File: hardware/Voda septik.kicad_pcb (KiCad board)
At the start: 2 copper layers, 1 part, among them U1 ESP32-DevKitC-30

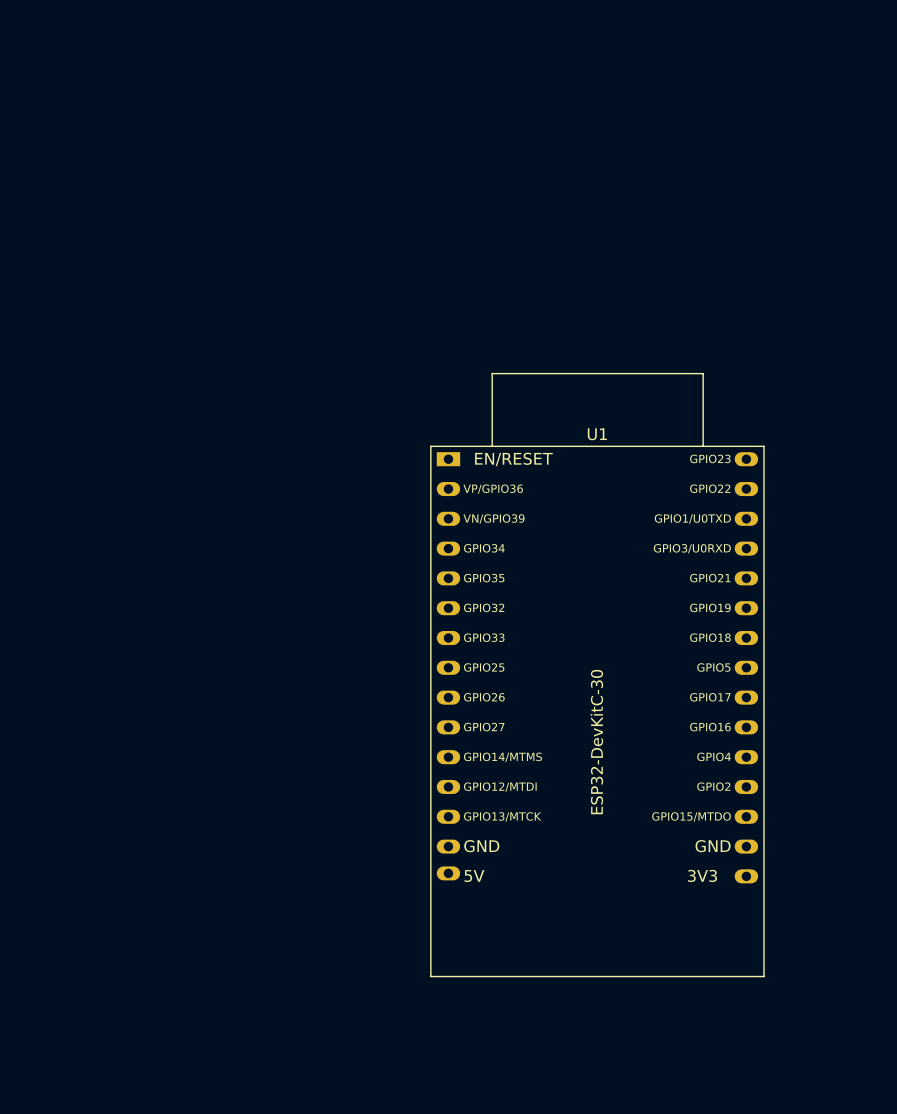
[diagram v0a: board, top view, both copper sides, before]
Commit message: Dokončení schématu a návrhu PCB o stavu, který byl poslán do výroby.
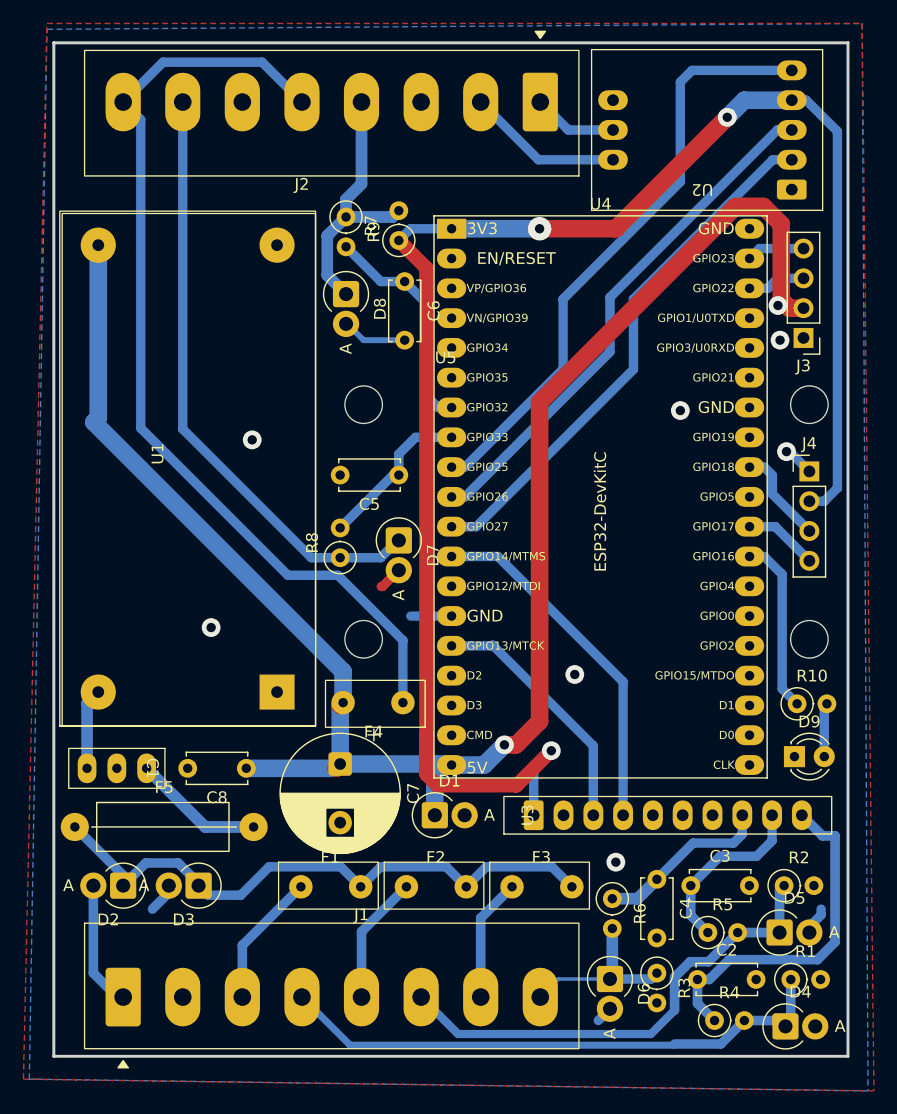
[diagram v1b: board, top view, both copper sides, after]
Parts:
- added C1: 100n, martin:Odruseni_3x_2.54mm, F.Cu at (98.8, 117.3)
- added C2: 100n, Capacitor_THT:C_Disc_D5.0mm_W2.5mm_P5.00mm, F.Cu at (145.7, 135.3)
- added C3: 100n, Capacitor_THT:C_Disc_D5.0mm_W2.5mm_P5.00mm, F.Cu at (145.2, 127.3)
- added C4: 100n, Capacitor_THT:C_Disc_D5.0mm_W2.5mm_P5.00mm, F.Cu at (142.3, 126.8)
- added C5: 1n, Capacitor_THT:C_Disc_D5.0mm_W2.5mm_P5.00mm, F.Cu at (120.3, 92.3)
- added C6: 100p, Capacitor_THT:C_Disc_D5.0mm_W2.5mm_P5.00mm, F.Cu at (120.8, 75.8)
- added C7: 470u, Capacitor_THT:CP_Radial_D10.0mm_P5.00mm, F.Cu at (115.3, 117.0)
- added C8: 100n, Capacitor_THT:C_Disc_D5.0mm_W2.5mm_P5.00mm, F.Cu at (107.3, 117.3)
- added D1: BZW04-5V8, Diode_THT:D_DO-15_P2.54mm_Vertical_AnodeUp, F.Cu at (123.3, 121.3)
- added D2: 1N4007, Diode_THT:D_DO-15_P2.54mm_Vertical_AnodeUp, F.Cu at (96.8, 127.3)
- added D3: BZW06-26, Diode_THT:D_DO-15_P2.54mm_Vertical_AnodeUp, F.Cu at (103.2, 127.3)
- added D4: BZW04-5V8, Diode_THT:D_DO-15_P2.54mm_Vertical_AnodeUp, F.Cu at (153.2, 139.3)
- added D5: BZW04-5V8, Diode_THT:D_DO-15_P2.54mm_Vertical_AnodeUp, F.Cu at (152.7, 131.3)
- added D6: BZW04-5V8, Diode_THT:D_DO-15_P2.54mm_Vertical_AnodeUp, F.Cu at (138.3, 135.3)
- added D7: BZW04-5V8, Diode_THT:D_DO-15_P2.54mm_Vertical_AnodeUp, F.Cu at (120.3, 97.9)
- added D8: BZW04-5V8, Diode_THT:D_DO-15_P2.54mm_Vertical_AnodeUp, F.Cu at (115.8, 76.9)
- added D9: LED, LED_THT:LED_D3.0mm, F.Cu at (154.0, 116.3)
- added F1: 50mA, martin:Fuse_Disc_D8.3_W3.8_P5.1, F.Cu at (111.9, 127.5)
- added F2: 50mA, martin:Fuse_Disc_D8.3_W3.8_P5.1, F.Cu at (120.9, 127.5)
- added F3: 50mA, martin:Fuse_Disc_D8.3_W3.8_P5.1, F.Cu at (129.9, 127.5)
- added F4: 50mA, martin:Fuse_Disc_D8.3_W3.8_P5.1, F.Cu at (120.6, 111.8)
- added F5: 0,5A, martin:Fuse_Axial_L11mm_D3.9mm_P15.24mm_Horizontal, F.Cu at (92.7, 122.3)
- added J1: Napájení a 4-20mA senzory, martin:Svorky_EB147A_8_5.08, F.Cu at (96.8, 136.8)
- added J2: Screw_Terminal_01x09, martin:Svorky_EB147A_8_5.08, F.Cu at (132.3, 60.5)
- added J3: Display LCD I2C, Connector_PinHeader_2.54mm:PinHeader_1x04_P2.54mm_Vertical, F.Cu at (154.8, 80.7)
- added J4: Display TM1637, Connector_PinHeader_2.54mm:PinHeader_1x04_P2.54mm_Vertical, F.Cu at (155.3, 92.0)
- added R1: 100R, Resistor_THT:R_Axial_DIN0207_L6.3mm_D2.5mm_P2.54mm_Vertical, F.Cu at (153.7, 135.3)
- added R10: 330R, Resistor_THT:R_Axial_DIN0207_L6.3mm_D2.5mm_P2.54mm_Vertical, F.Cu at (154.2, 111.8)
- added R2: 100R, Resistor_THT:R_Axial_DIN0207_L6.3mm_D2.5mm_P2.54mm_Vertical, F.Cu at (153.1, 127.3)
- added R3: 100R, Resistor_THT:R_Axial_DIN0207_L6.3mm_D2.5mm_P2.54mm_Vertical, F.Cu at (142.3, 134.8)
- added R4: 2k2, Resistor_THT:R_Axial_DIN0207_L6.3mm_D2.5mm_P2.54mm_Vertical, F.Cu at (147.2, 138.8)
- added R5: 2k2, Resistor_THT:R_Axial_DIN0207_L6.3mm_D2.5mm_P2.54mm_Vertical, F.Cu at (146.6, 131.3)
- added R6: 2k2, Resistor_THT:R_Axial_DIN0207_L6.3mm_D2.5mm_P2.54mm_Vertical, F.Cu at (138.5, 128.5)
- added R7: 2k2, Resistor_THT:R_Axial_DIN0207_L6.3mm_D2.5mm_P2.54mm_Vertical, F.Cu at (120.3, 72.3)
- added R8: 3k9, Resistor_THT:R_Axial_DIN0207_L6.3mm_D2.5mm_P2.54mm_Vertical, F.Cu at (115.3, 99.4)
- added R9: 56R, Resistor_THT:R_Axial_DIN0207_L6.3mm_D2.5mm_P2.54mm_Vertical, F.Cu at (115.8, 70.3)
- added U1: DC-DC 24V -> 5V, martin:LM2596 DC-DC HW-411, F.Cu at (109.9, 110.8)
- added U2: MAX3485-modul, martin:MAX3485-modul, F.Cu at (153.8, 68.0)
- added U3: ADS1115IDGS, martin:ADS1115_modul_vertical, F.Cu at (131.8, 121.3)
- added U5: CA56-12CGKWA, martin:DISPLAY_clok_MOUNT_4xM3, F.Cu at (117.3, 86.3)
- U4: renamed from U1; value ESP32-DevKitC-30 -> ESP32-DevKitC; footprint martin:ESP32-DevKitC-30 -> PCM_Espressif:ESP32-DevKitC
- moved U4 19.7 mm to (124.8, 71.3)
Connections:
- U4 pad 1: unconnected-(U1-CHIP_PU-Pad1) -> +3.3V
- U4 pad 10: unconnected-(U1-ADC2_CH7/GPIO27-Pad10) -> Net-(U2-RXD)
- U4 pad 11: unconnected-(U1-MTMS/GPIO14/ADC2_CH6-Pad11) -> Net-(U2-TXD)
- U4 pad 12: unconnected-(U1-MTDI/GPIO12/ADC2_CH5-Pad12) -> Net-(U3-SDA)
- U4 pad 14: unconnected-(U1-GND-Pad14) -> GND
- U4 pad 15: unconnected-(U1-5V-Pad15) -> Net-(U3-SCL)
- U4 pad 19: unconnected-(U1-ADC2_CH2/GPIO2-Pad19) -> +5V
- U4 pad 24: Net-(U1-GPIO18) -> unconnected-(U4-ADC2_CH2/GPIO2-Pad24)
- U4 pad 27: unconnected-(U1-U0RXD/GPIO3-Pad27) -> Net-(U4-GPIO16)
- U4 pad 28: unconnected-(U1-U0TXD/GPIO1-Pad28) -> Net-(J4-CLK)
- U4 pad 30: unconnected-(U1-GPIO23-Pad30) -> Net-(J4-DIO)
- U4 pad 7: unconnected-(U1-32K_XN/GPIO33/ADC1_CH5-Pad7) -> /teploměry
- U4 pad 8: unconnected-(U1-DAC_1/ADC2_CH8/GPIO25-Pad8) -> /průtok
- U4 pad 9: unconnected-(U1-DAC_2/ADC2_CH9/GPIO26-Pad9) -> Net-(U2-EN)
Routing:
- net +3.3V: track 0.00 -> 157.3 mm, vias 0 -> 3
- net +5V: track 0.00 -> 151.6 mm, vias 0 -> 2
- net Net-(J2-1wire+5V): track 0.00 -> 81.6 mm
- net Net-(D7-K): track 0.00 -> 51.6 mm
- net Net-(D2-K): track 0.00 -> 51.5 mm
- net Net-(U2-EN): track 0.00 -> 50.3 mm
- net Net-(D4-K): track 0.00 -> 48.2 mm
- net Net-(U2-TXD): track 0.00 -> 45.5 mm
- net Net-(U2-RXD): track 0.00 -> 44.7 mm
- net Net-(D5-K): track 0.00 -> 41.3 mm
- net Net-(U3-SDA): track 0.00 -> 30.4 mm
- net /hladina 4-20mA: track 0.00 -> 29.8 mm
- net Net-(D8-K): track 0.00 -> 23.0 mm
- net Net-(U3-SCL): track 0.00 -> 21.6 mm
- net GND: track 0.00 -> 20.6 mm, vias 0 -> 7
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- added copper zone on B.Cu, net GND
- added copper zone on F.Cu, net GND
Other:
- board outline added: 67.7 x 86.4 mm
